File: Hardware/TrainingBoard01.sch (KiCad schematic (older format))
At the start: 14 parts, among them J1 Test_Point, J2 Test_Point

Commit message: Created Training Board
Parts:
- removed Conn1: AndersonPP, symbol MRDT_Connectors:AndersonPP
- removed J1: Test_Point, symbol MRDT_Connectors:Test_Point
- removed U?: LM2576D2TR4-3.3G, symbol LM2576D2TR4-3.3G:LM2576D2TR4-3.3G
- added U?: LM2576D2TR4-3.3G, symbol MRDT_Devices:LM2576D2TR4-3.3G
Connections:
- net +12V: now also U?.1 (VIN)
- net +3V3: now also U?.4 (FEEDBACK)
- net GND: now also U?.3 (GND), U?.5 (ON/OFF), U?.6 (TAB)
- net at L?.1: now also U?.2 (OUTPUT)
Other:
- moved on the sheet: C?, D5, D?, FB1, J2, J?, L?, R1, R?

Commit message: made board
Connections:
- net Power_Input: now reaches D?.1 (K), FB1.2
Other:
- note added: "Sheet 1: Power"
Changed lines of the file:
@@
 	1    0    0    -1
 $EndComp
+Text Notes 9575 6975 2    200  ~ 40
+Sheet 1: Power
+Text GLabel 2700 3100 0    50   Input ~ 0
+Power_Input
+Wire Wire Line
+	2700 3100 3000 3100
+Connection ~ 3000 3100
 $EndSCHEMATC

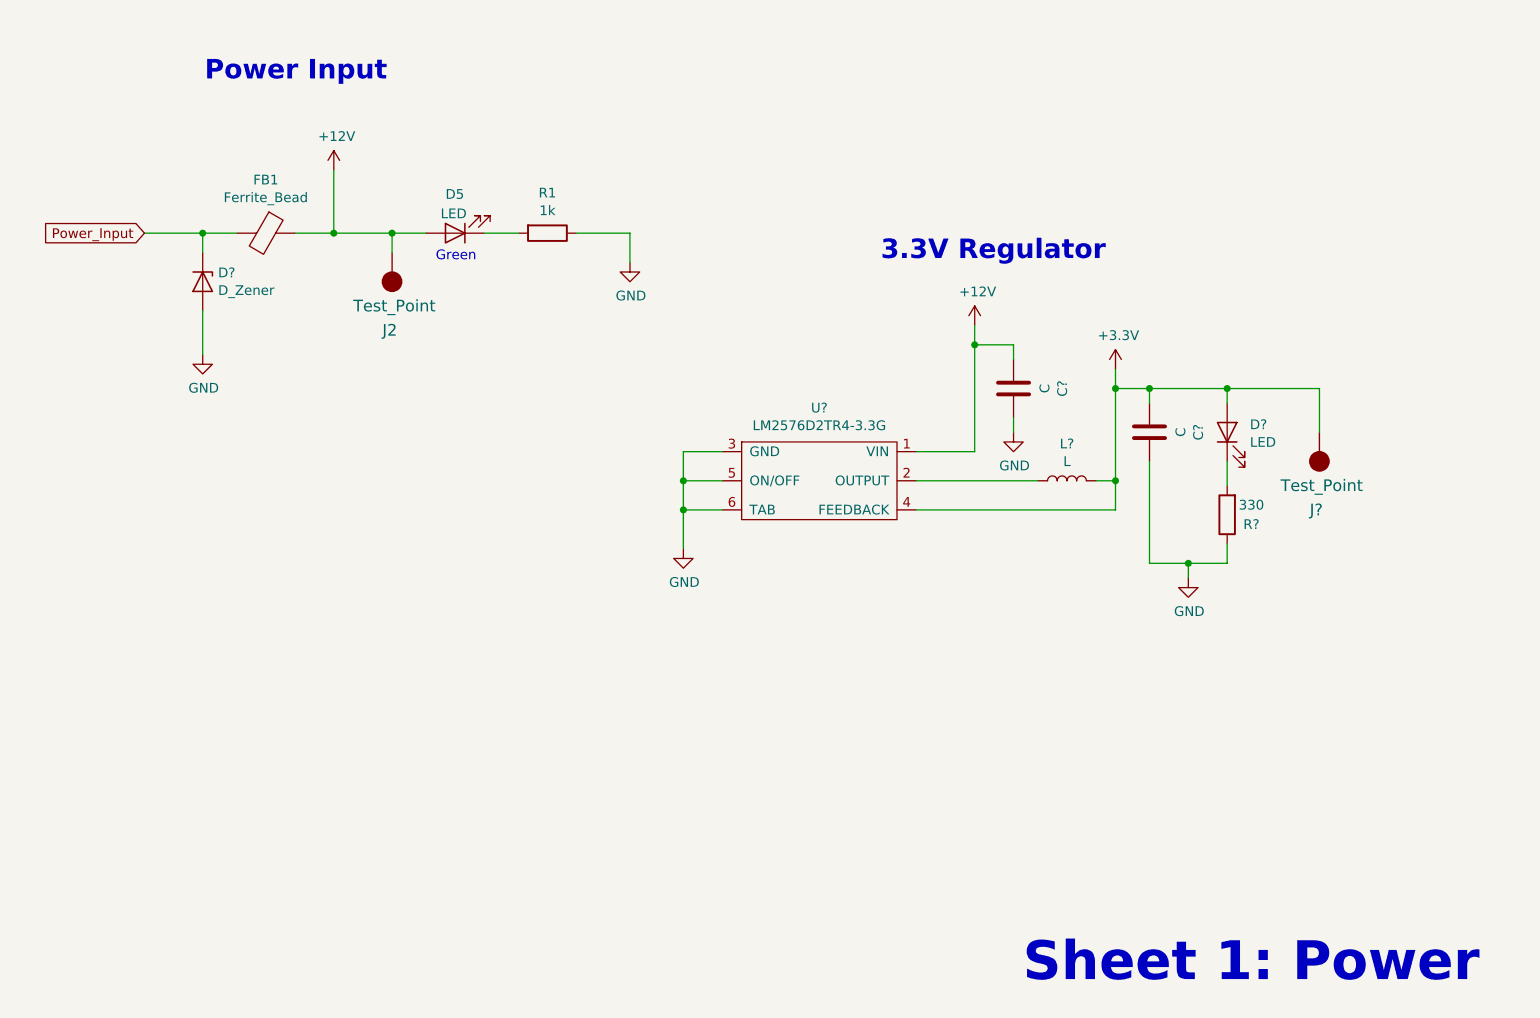
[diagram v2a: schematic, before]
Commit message: Added values for buck components
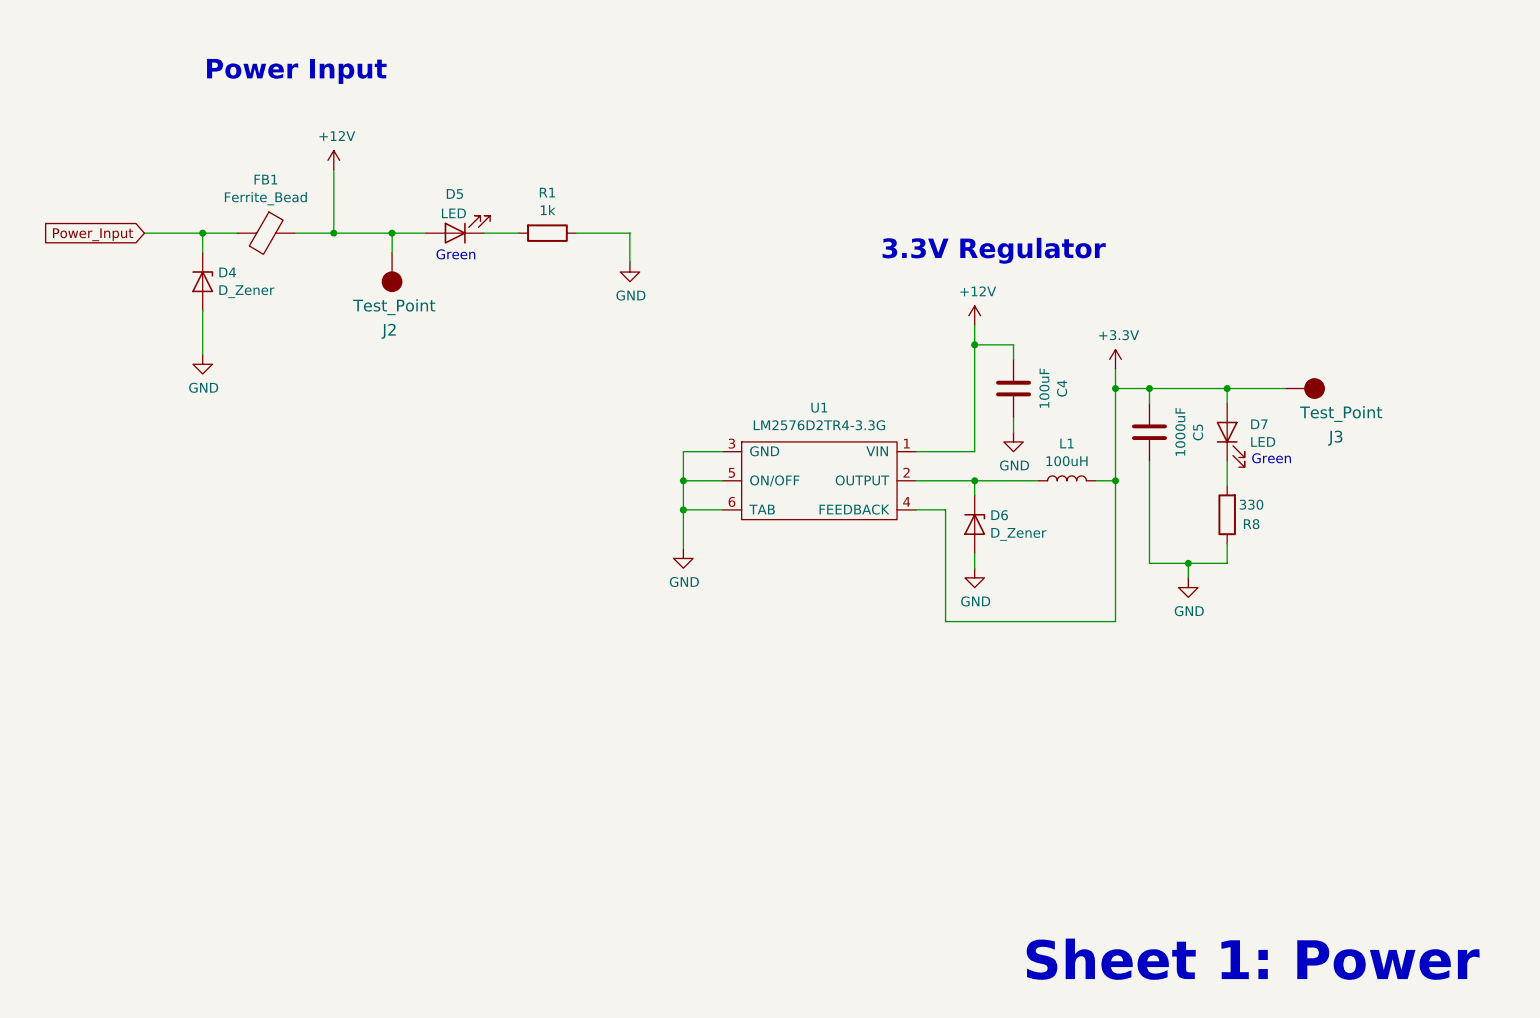
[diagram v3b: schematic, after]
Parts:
- added D6: D_Zener, symbol Device:D_Zener
- C4: renamed from C?; value C -> 100uF
- C5: renamed from C?; value C -> 1000uF
- L1: renamed from L?; value L -> 100uH
- gave numbers to parts that had none: 5
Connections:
- net GND: now also D6.2 (A)
- net at L1.1, U1.2 (OUTPUT): now also D6.1 (K)
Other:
- moved on the sheet: J3
